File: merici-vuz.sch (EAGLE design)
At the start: 46 parts, among them IC1 MEGA328-PB, IC2 MCP73831, IC3 LE33, Q1 3,6864 MHz, T1 IRF7306

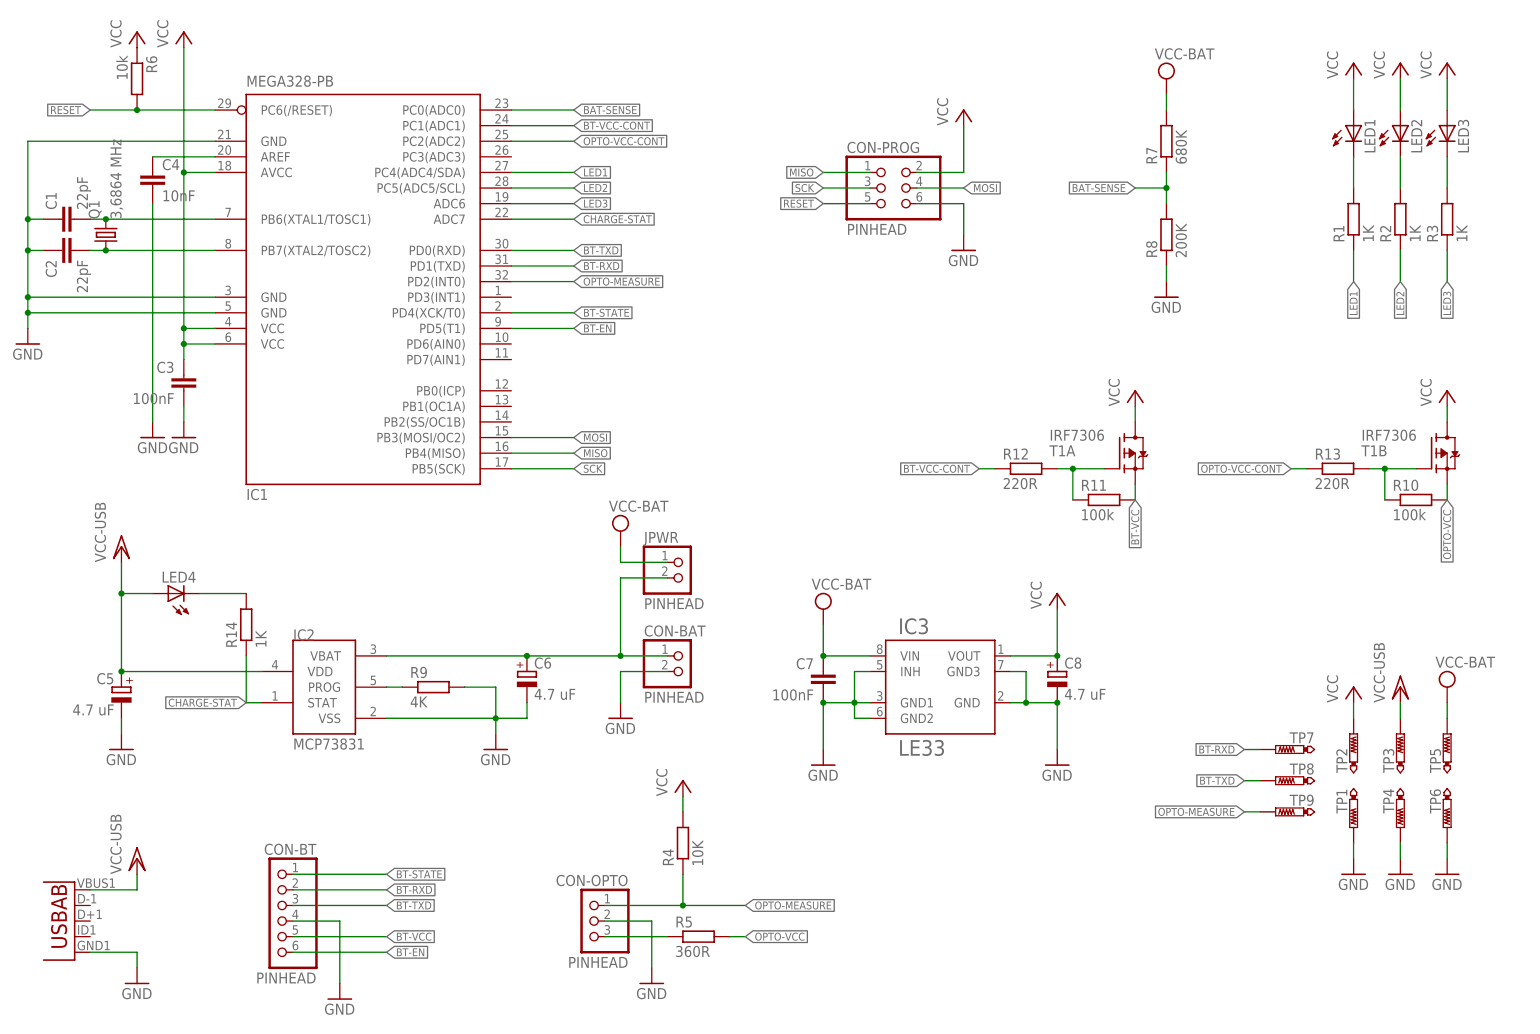
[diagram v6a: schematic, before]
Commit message: Eagle 9.0 & on & off buttons.
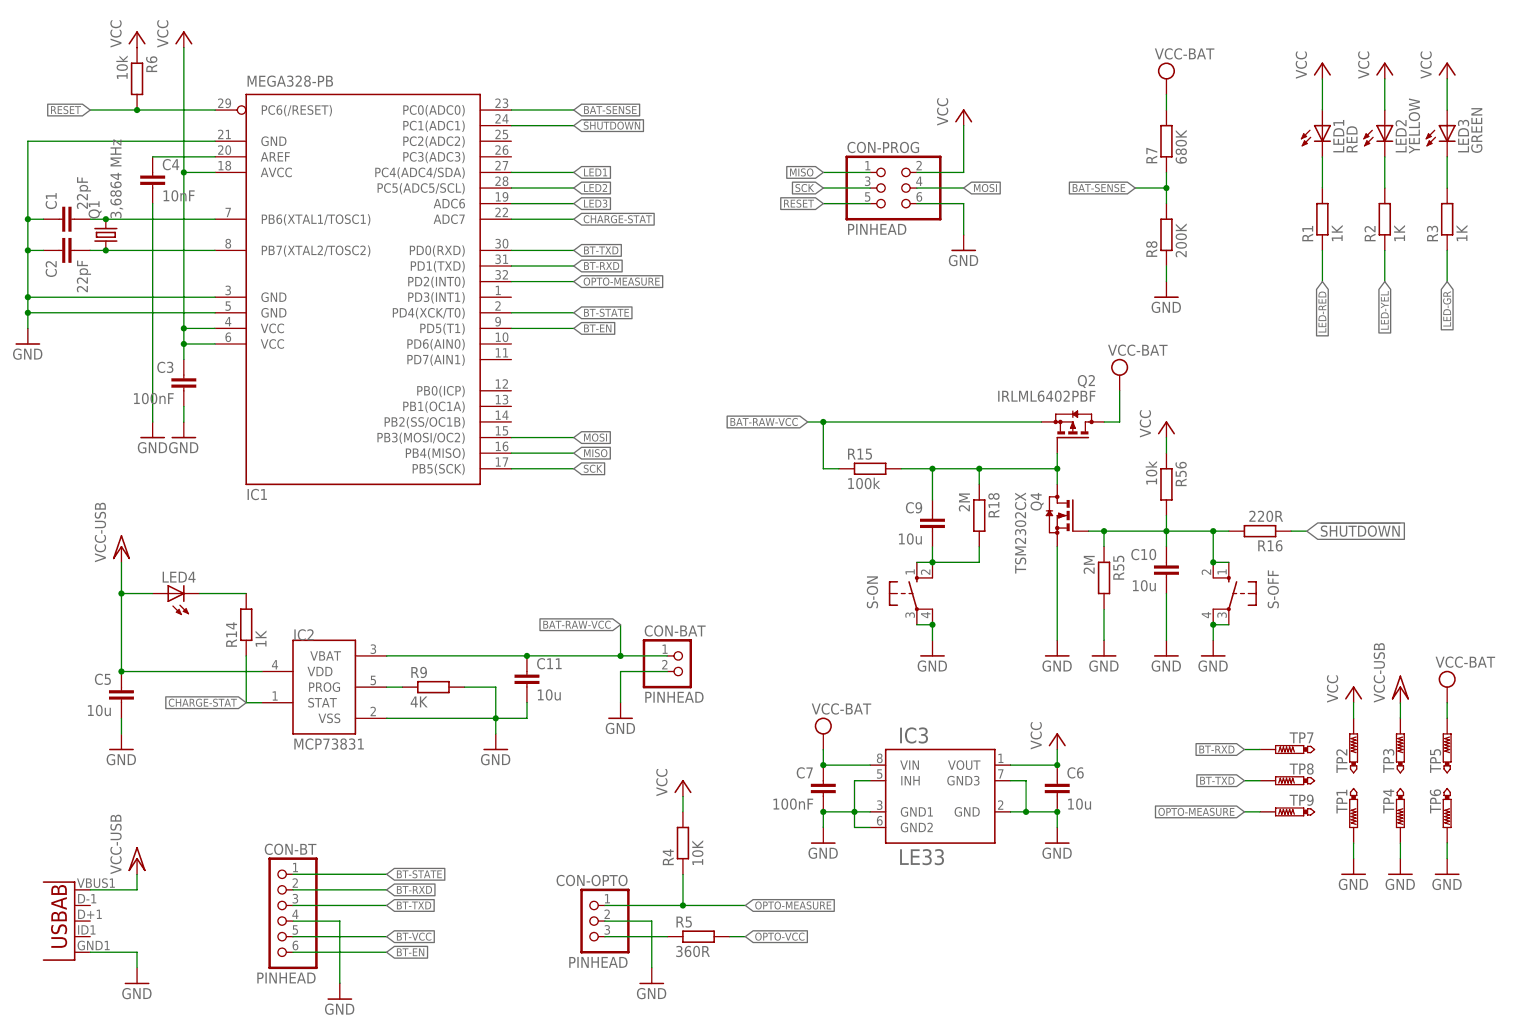
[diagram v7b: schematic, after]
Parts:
- removed C8: 4.7 uF, rcl:CPOL-EUE1.8-4
- removed JPWR: PINHEAD, pinhead:PINHD-1X2
- removed R10, R11: 100k, rcl:R-EU_R0805
- removed R12, R13: 220R, rcl:R-EU_R0805
- removed T1: IRF7306, transistor-fet:IRF7306
- added C10, C11, C9: 10u, rcl:C-EUC0805
- added Q2: IRLML6402PBF, transistor-small-signal:BSS84
- added Q4: TSM2302CX, transistor-small-signal:BSS123
- added R15: 100k, rcl:R-EU_R0805
- added R16: 220R, rcl:R-EU_R0805
- added R18, R55: 2M, rcl:R-EU_R0805
- added R56: 10k, rcl:R-EU_R0805
- added S-OFF, S-ON: (no value), switch-omron:10-XX
- C5, C6: value 4.7 uF -> 10u; device rcl:CPOL-EUE1.8-4 -> rcl:C-EUC0805
- LED1: value (none) -> RED
- LED2: value (none) -> YELLOW
- LED3: value (none) -> GREEN
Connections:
- removed net BT-VCC-CONT: IC1.PC1(ADC1), R12.1
- removed net BT-VCC-CONT_: R11.1, R12.2, T1A.G
- removed net N$7: C6.+, CON-BAT.1, IC2.VBAT, JPWR.2
- removed net OPTO-VCC-CONT: IC1.PC2(ADC2), R13.1
- removed net OPTO-VCC-CONT_: R10.1, R13.2, T1B.G
- new net !SHUTDOWN: IC1.PC1(ADC1), R16.1
- new net !SHUTDOWN_INT: C10.1, Q4.G, R16.2, R55.1, R56.2, S-OFF.S, S-OFF.S1
- new net BAT-RAW-VCC: C11.1, CON-BAT.1, IC2.VBAT, Q2.S, R15.1
- new net LED-GR: R3.1
- new net LED-RED: R1.1
- new net LED-YEL: R2.1
- new net START_BUTTON: C9.2, R18.2, S-ON.S, S-ON.S1
- new net START_GATE: C9.1, Q2.G, Q4.D, R15.2, R18.1
- net BT-VCC: no longer R11.2, T1A.S
- net GND: now also C10.2, C11.2, C5.2, C6.2, Q4.S, R55.2, S-OFF.P, S-OFF.P1, S-ON.P, S-ON.P1; no longer C5.-, C6.-, C8.-
- net LED1: no longer R1.1
- net LED2: no longer R2.1
- net LED3: no longer R3.1
- net OPTO-VCC: no longer R10.2, T1B.S
- net VCC: now also C6.1, Q2.D, R56.1; no longer C8.+, T1A.D, T1B.D
- net VCC-BAT: no longer JPWR.1
- net VCC/2: now also C5.1; no longer C5.+
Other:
- moved on the sheet: C7, IC3, LED1, LED2, R1, R2

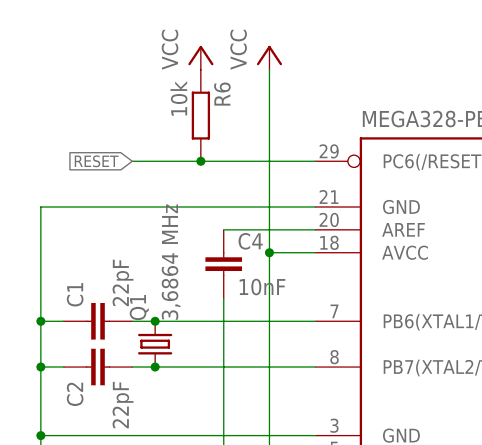
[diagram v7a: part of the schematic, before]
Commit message: Reset -> !reset.
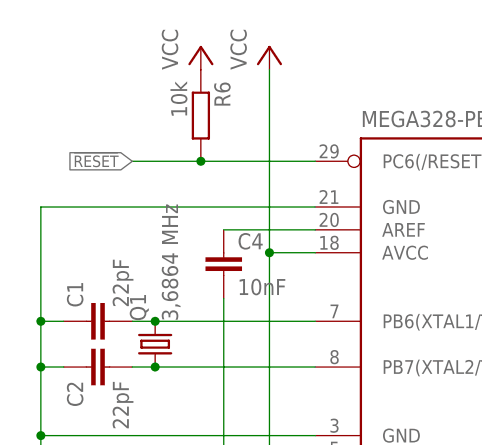
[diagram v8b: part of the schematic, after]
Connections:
- new net !RESET: IC1.PC6(/RESET), R6.2
- net RESET: no longer IC1.PC6(/RESET), R6.2
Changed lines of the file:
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@@
 <grid distance="2.54" unitdist="mm" unit="mm" style="lines" multiple="1" display="no" altdistance="0.254" altunitdist="mm" altunit="mm"/>
 <layers>
-<layer number="1" name="Top" color="4" fill="1" visible="yes" active="no"/>
-<layer number="2" name="Route2" color="1" fill="3" visible="yes" active="no"/>
-<layer number="3" name="Route3" color="4" fill="3" visible="yes" active="no"/>
-<layer number="4" name="Route4" color="1" fill="4" visible="yes" active="no"/>
-<layer number="5" name="Route5" color="4" fill="4" visible="yes" active="no"/>
-<layer number="6" name="Route6" color="1" fill="8" visible="yes" active="no"/>
-<layer number="7" name="Route7" color="4" fill="8" visible="yes" active="no"/>
-<layer number="8" name="Route8" color="1" fill="2" visible="yes" active="no"/>
-<layer number="9" name="Route9" color="4" fill="2" visible="yes" active="no"/>
-<layer number="10" name="Route10" color="1" fill="7" visible="yes" active="no"/>
-<layer number="11" name="Route11" color="4" fill="7" visible="yes" active="no"/>
-<layer number="12" name="Route12" color="1" fill="5" visible="yes" active="no"/>
-<layer number="13" name="Route13" color="4" fill="5" visible="yes" active="no"/>
-<layer number="14" name="Route14" color="1" fill="6" visible="yes" active="no"/>
-<layer number="15" name="Route15" color="4" fill="6" visible="yes" active="no"/>
-<layer number="16" name="Bottom" color="1" fill="1" visible="yes" active="no"/>
-<layer number="17" name="Pads" color="2" fill="1" visible="yes" active="no"/>
-<layer number="18" name="Vias" color="2" fill="1" visible="yes" active="no"/>
-<layer number="19" name="Unrouted" color="6" fill="1" visible="yes" active="no"/>
-<layer number="20" name="Dimension" color="15" fill="1" visible="yes" active="no"/>
-<layer number="21" name="tPlace" color="7" fill="1" visible="yes" active="no"/>
-<layer number="22" name="bPlace" color="7" fill="1" visible="yes" active="no"/>
-<layer number="23" name="tOrigins" color="15" fill="1" visible="yes" active="no"/>
-<layer number="24" name="bOrigins" color="15" fill="1" visible="yes" active="no"/>
-<layer number="25" name="tNames" color="7" fill="1" visible="yes" active="no"/>
-<layer number="26" name="bNames" color="7" fill="1" visible="yes" active="no"/>
-<layer number="27" name="tValues" color="7" fill="1" visible="yes" active="no"/>
-<layer number="28" name="bValues" color="7" fill="1" visible="yes" active="no"/>
+<layer number="1" name="Top" color="4" fill="1" visible="no" active="no"/>
+<layer number="2" name="Route2" color="1" fill="3" visible="no" active="no"/>
+<layer number="3" name="Route3" color="4" fill="3" visible="no" active="no"/>
+<layer number="4" name="Route4" color="1" fill="4" visible="no" active="no"/>
+<layer number="5" name="Route5" color="4" fill="4" visible="no" active="no"/>
+<layer number="6" name="Route6" color="1" fill="8" visible="no" active="no"/>
+<layer number="7" name="Route7" color="4" fill="8" visible="no" active="no"/>
+<layer number="8" name="Route8" color="1" fill="2" visible="no" active="no"/>
+<layer number="9" name="Route9" color="4" fill="2" visible="no" active="no"/>
+<layer number="10" name="Route10" color="1" fill="7" visible="no" active="no"/>
+<layer number="11" name="Route11" color="4" fill="7" visible="no" active="no"/>
+<layer number="12" name="Route12" color="1" fill="5" visible="no" active="no"/>
+<layer number="13" name="Route13" color="4" fill="5" visible="no" active="no"/>
+<layer number="14" name="Route14" color="1" fill="6" visible="no" active="no"/>
+<layer number="15" name="Route15" color="4" fill="6" visible="no" active="no"/>
+<layer number="16" name="Bottom" color="1" fill="1" visible="no" active="no"/>
+<layer number="17" name="Pads" color="2" fill="1" visible="no" active="no"/>
+<layer number="18" name="Vias" color="2" fill="1" visible="no" active="no"/>
+<layer number="19" name="Unrouted" color="6" fill="1" visible="no" active="no"/>
+<layer number="20" name="Dimension" color="15" fill="1" visible="no" active="no"/>
+<layer number="21" name="tPlace" color="7" fill="1" visible="no" active="no"/>
+<layer number="22" name="bPlace" color="7" fill="1" visible="no" active="no"/>
+<layer number="23" name="tOrigins" color="15" fill="1" visible="no" active="no"/>
+<layer number="24" name="bOrigins" color="15" fill="1" visible="no" active="no"/>
+<layer number="25" name="tNames" color="7" fill="1" visible="no" active="no"/>
+<layer number="26" name="bNames" color="7" fill="1" visible="no" active="no"/>
+<layer number="27" name="tValues" color="7" fill="1" visible="no" active="no"/>
+<layer number="28" name="bValues" color="7" fill="1" visible="no" active="no"/>
 <layer number="29" name="tStop" color="7" fill="3" visible="no" active="no"/>
 <layer number="30" name="bStop" color="7" fill="6" visible="no" active="no"/>
@@
 <layer number="35" name="tGlue" color="7" fill="4" visible="no" active="no"/>
 <layer number="36" name="bGlue" color="7" fill="5" visible="no" active="no"/>
-<layer number="37" name="tTest" color="7" fill="1" visible="yes" active="no"/>
-<layer number="38" name="bTest" color="7" fill="1" visible="yes" active="no"/>
+<layer number="37" name="tTest" color="7" fill="1" visible="no" active="no"/>
+<layer number="38" name="bTest" color="7" fill="1" visible="no" active="no"/>
 <layer number="39" name="tKeepout" color="4" fill="11" visible="no" active="no"/>
 <layer number="40" name="bKeepout" color="1" fill="11" visible="no" active="no"/>
@@
 <layer number="44" name="Drills" color="7" fill="1" visible="no" active="no"/>
 <layer number="45" name="Holes" color="7" fill="1" visible="no" active="no"/>
-<layer number="46" name="Milling" color="3" fill="1" visible="yes" active="no"/>
-<layer number="47" name="Measures" color="7" fill="1" visible="yes" active="no"/>
-<layer number="48" name="Document" color="7" fill="1" visible="yes" active="no"/>
-<layer number="49" name="Reference" color="7" fill="1" visible="yes" active="no"/>
-<layer number="50" name="dxf" color="7" fill="1" visible="yes" active="no"/>
-<layer number="51" name="tDocu" color="7" fill="1" visible="yes" active="no"/>
-<layer number="52" name="bDocu" color="7" fill="1" visible="yes" active="no"/>
-<layer number="53" name="tGND_GNDA" color="7" fill="9" visible="yes" active="no"/>
-<layer number="54" name="bGND_GNDA" color="1" fill="9" visible="yes" active="no"/>
-<layer number="55" name="tPotisk" color="7" fill="1" visible="yes" active="no"/>
-<layer number="56" name="wert" color="7" fill="1" visible="yes" active="no"/>
-<layer number="57" name="tCAD" color="7" fill="1" visible="yes" active="no"/>
-<layer number="58" name="bNC" color="7" fill="1" visible="yes" active="no"/>
-<layer number="59" name="tCarbon" color="7" fill="1" visible="yes" active="no"/>
-<layer number="60" name="bCarbon" color="7" fill="1" visible="yes" active="no"/>
-<layer number="61" name="stand" color="7" fill="1" visible="yes" active="no"/>
+<layer number="46" name="Milling" color="3" fill="1" visible="no" active="no"/>
+<layer number="47" name="Measures" color="7" fill="1" visible="no" active="no"/>
+<layer number="48" name="Document" color="7" fill="1" visible="no" active="no"/>
+<layer number="49" name="Reference" color="7" fill="1" visible="no" active="no"/>
+<layer number="50" name="dxf" color="7" fill="1" visible="no" active="no"/>
+<layer number="51" name="tDocu" color="7" fill="1" visible="no" active="no"/>
+<layer number="52" name="bDocu" color="7" fill="1" visible="no" active="no"/>
+<layer number="53" name="tGND_GNDA" color="7" fill="9" visible="no" active="no"/>
+<layer number="54" name="bGND_GNDA" color="1" fill="9" visible="no" active="no"/>
+<layer number="55" name="tPotisk" color="7" fill="1" visible="no" active="no"/>
+<layer number="56" name="wert" color="7" fill="1" visible="no" active="no"/>
+<layer number="57" name="tCAD" color="7" fill="1" visible="no" active="no"/>
+<layer number="58" name="bNC" color="7" fill="1" visible="no" active="no"/>
+<layer number="59" name="tCarbon" color="7" fill="1" visible="no" active="no"/>
+<layer number="60" name="bCarbon" color="7" fill="1" visible="no" active="no"/>
+<layer number="61" name="stand" color="7" fill="1" visible="no" active="no"/>
 <layer number="88" name="SimResults" color="9" fill="1" visible="yes" active="yes"/>
 <layer number="89" name="SimProbes" color="9" fill="1" visible="yes" active="yes"/>
@@
 <label x="142.24" y="142.24" size="1.27" layer="95" rot="R180" xref="yes"/>
 </segment>
-<segment>
-<pinref part="IC1" gate="G$1" pin="PC6(/RESET)"/>
-<pinref part="R6" gate="G$1" pin="2"/>
-<wire x1="43.18" y1="157.48" x2="30.48" y2="157.48" width="0.1524" layer="91"/>
-<wire x1="30.48" y1="157.48" x2="22.86" y2="157.48" width="0.1524" layer="91"/>
-<junction x="30.48" y="157.48"/>
-<label x="22.86" y="157.48" size="1.27" layer="95" rot="R180" xref="yes"/>
-</segment>
 </net>
 <net name="MOSI" class="0">
@@
 </segment>
 </net>
+<net name="!RESET" class="0">
+<segment>
+<pinref part="IC1" gate="G$1" pin="PC6(/RESET)"/>
+<pinref part="R6" gate="G$1" pin="2"/>
+<wire x1="43.18" y1="157.48" x2="30.48" y2="157.48" width="0.1524" layer="91"/>
+<wire x1="30.48" y1="157.48" x2="22.86" y2="157.48" width="0.1524" layer="91"/>
+<junction x="30.48" y="157.48"/>
+<label x="22.86" y="157.48" size="1.27" layer="95" rot="R180" xref="yes"/>
+</segment>
+</net>
